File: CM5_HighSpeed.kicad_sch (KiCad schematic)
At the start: 60 parts, among them J1 USB-C, J10 USB-C, J15 USB_C_Receptacle, J17 USB-C, J22 Conn_HDMI, J5 Conn_1x22_Female, J6 USB-C, U11 TUSB4041I, U12 RT9742SNGV, U13 TLV73311PDBV, U15 AP22653W6, U6 AP22653W6, Y1 ECS-2520MV-240-CN-TR

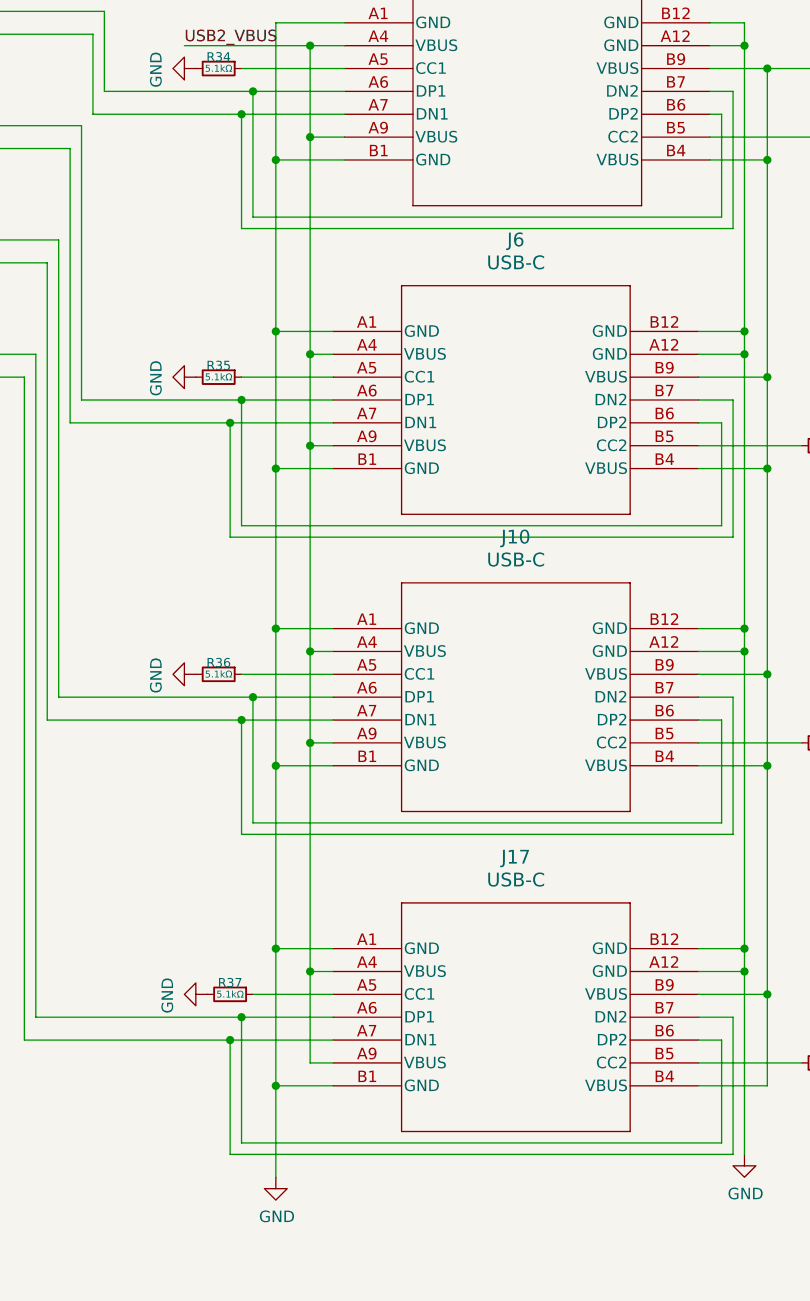
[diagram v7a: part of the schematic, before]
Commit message: Update thickness of traces, smaller fixes
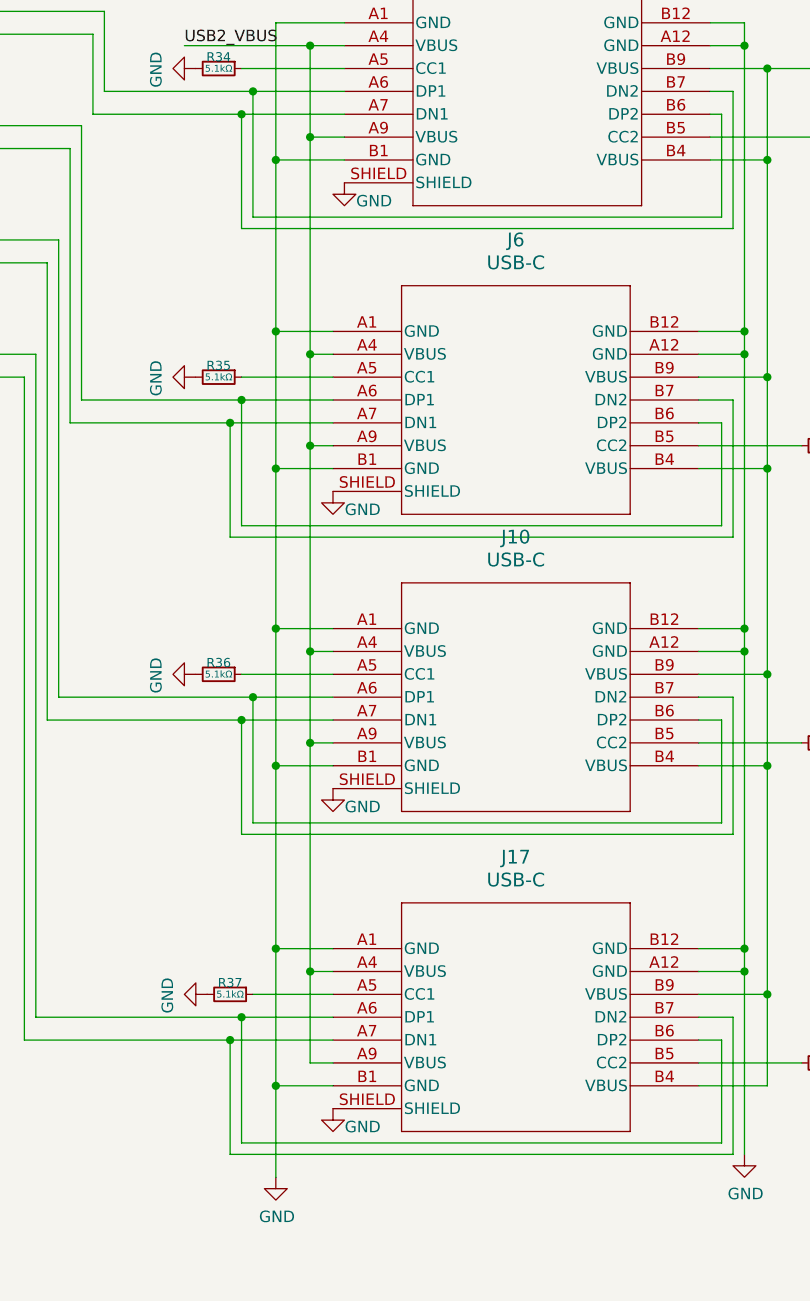
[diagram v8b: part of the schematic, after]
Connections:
- net GND: now also J1.SHIELD, J10.SHIELD, J17.SHIELD, J6.SHIELD
